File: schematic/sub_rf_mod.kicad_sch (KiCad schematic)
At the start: 36 parts, among them J4B1 Conn_01x08

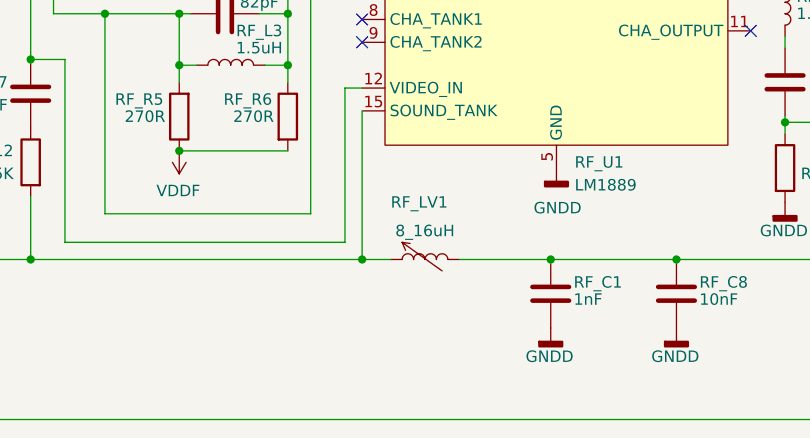
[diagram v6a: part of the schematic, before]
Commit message: added new libs for rest of the parts. some still need updating for correct parts, but for now they work. PCB import complete.
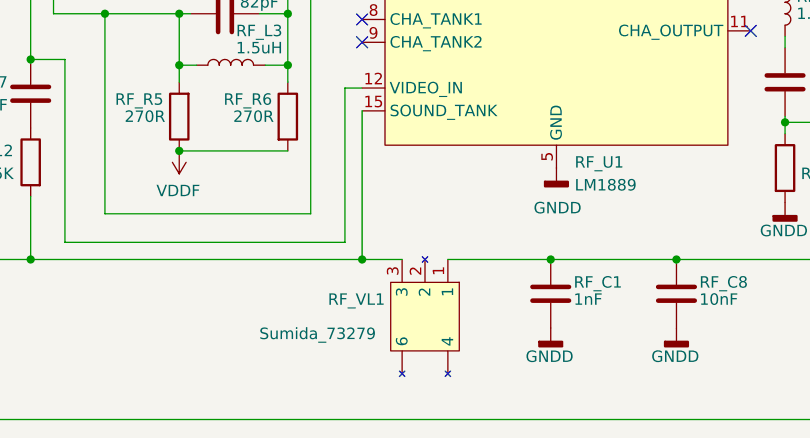
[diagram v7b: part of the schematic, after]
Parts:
- removed RF_LV1: 8_16uH, symbol Device:L_Trim
- added RF_VL1: Sumida_73279, Variable_Inductors:Sumida_73279, symbol Variable_Inductors:Sumida_73279
- RF_J1: footprint (none) -> RCJ-041:RCJ041
- RF_JP1: footprint Resistor_THT:R_Bare_Metal_Element_L16.3mm_W4.8mm_P15.30mm -> Resistor_THT:R_Axial_DIN0204_L3.6mm_D1.6mm_P7.62mm_Horizontal
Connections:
- net at RF_D2.1 (K), RF_R12.2, RF_U1.15 (SOUND_TANK): now also RF_VL1.3
- net at RF_C1.1, RF_C8.1, RF_JP1.1 (A)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: now also RF_VL1.1
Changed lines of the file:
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@@
     (stroke (width 0) (type default) (color 0 0 0 0))
   )
-  (wire (pts (xy 137.795 126.365) (xy 134.62 126.365))
+  (wire (pts (xy 134.62 126.365) (xy 139.065 126.365))
     (stroke (width 0) (type default) (color 0 0 0 0))
   )
@@
     (stroke (width 0) (type default) (color 0 0 0 0))
   )
+  (wire (pts (xy 144.145 126.365) (xy 155.575 126.365))
+    (stroke (width 0) (type default) (color 0 0 0 0))
+  )
   (wire (pts (xy 200.66 111.125) (xy 207.645 111.125))
     (stroke (width 0) (type default) (color 0 0 0 0))
@@
   )
   (wire (pts (xy 85.725 105.41) (xy 76.835 105.41))
-    (stroke (width 0) (type default) (color 0 0 0 0))
-  )
-  (wire (pts (xy 145.415 126.365) (xy 155.575 126.365))
     (stroke (width 0) (type default) (color 0 0 0 0))
   )
@@
     )
     (pin "1")
-  )
-  (symbol (lib_id "Device:L_Trim") (at 141.605 126.365 90) (unit 1)
-    (in_bom yes) (on_board yes)
-    (property "Reference" "RF_LV1" (id 0) (at 140.97 120.015 90))
-    (property "Value" "8_16uH" (id 1) (at 141.605 123.19 90))
-    (property "Footprint" "" (id 2) (at 141.605 126.365 0)
-      (effects (font (size 1.27 1.27)) hide)
-    )
-    (property "Datasheet" "~" (id 3) (at 141.605 126.365 0)
-      (effects (font (size 1.27 1.27)) hide)
-    )
-    (pin "1")
-    (pin "2")
   )
   (symbol (lib_id "Device:C") (at 119.38 92.075 90) (mirror x) (unit 1)
@@
       (effects (font (size 1.27 1.27)) (justify right))
     )
-    (property "Footprint" "Resistor_THT:R_Bare_Metal_Element_L16.3mm_W4.8mm_P15.30mm" (id 2) (at 153.67 59.69 0)
+    (property "Footprint" "Resistor_THT:R_Axial_DIN0204_L3.6mm_D1.6mm_P7.62mm_Horizontal" (id 2) (at 153.67 59.69 0)
       (effects (font (size 1.27 1.27)) hide)
     )
@@
       (effects (font (size 1.27 1.27)) (justify right))
     )
-    (property "Footprint" "" (id 2) (at 226.695 111.125 0)
+    (property "Footprint" "RCJ-041:RCJ041" (id 2) (at 226.695 111.125 0)
       (effects (font (size 1.27 1.27)) hide)
     )
@@
     (pin "2")
   )
+  (symbol (lib_id "Variable_Inductors:Sumida_73279") (at 141.605 132.715 270) (unit 1)
+    (in_bom yes) (on_board yes)
+    (property "Reference" "RF_VL1" (id 0) (at 130.81 130.81 90)
+      (effects (font (size 1.27 1.27)) (justify left))
+    )
+    (property "Value" "Sumida_73279" (id 1) (at 123.19 134.62 90)
+      (effects (font (size 1.27 1.27)) (justify left))
+    )
+    (property "Footprint" "Variable_Inductors:Sumida_73279" (id 2) (at 146.685 132.715 0)
+      (effects (font (size 1.27 1.27)) hide)
+    )
+    (property "Datasheet" "" (id 3) (at 146.685 132.715 0)
+      (effects (font (size 1.27 1.27)) hide)
+    )
+    (pin "")
+    (pin "")
+    (pin "1")
+    (pin "2")
+    (pin "3")
+  )
   (symbol (lib_id "Device:C_Polarized") (at 39.37 53.975 0) (unit 1)
